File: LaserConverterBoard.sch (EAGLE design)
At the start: 49 parts, among them J10 24V, J11 FAN, J12 E-STOP, J3 04-JST-B4B-XH-A, J4 04-JST-B4B-XH-A, J5 04-JST-B4B-XH-A, J6 X, J7 Y, J8 Z-STOP, Q1 FDN5630, Q2 FDN5630, U10 REE-0505S, Y1 POLOLU_A4988, Y2 POLOLU_A4988, Y3 POLOLU_A4988

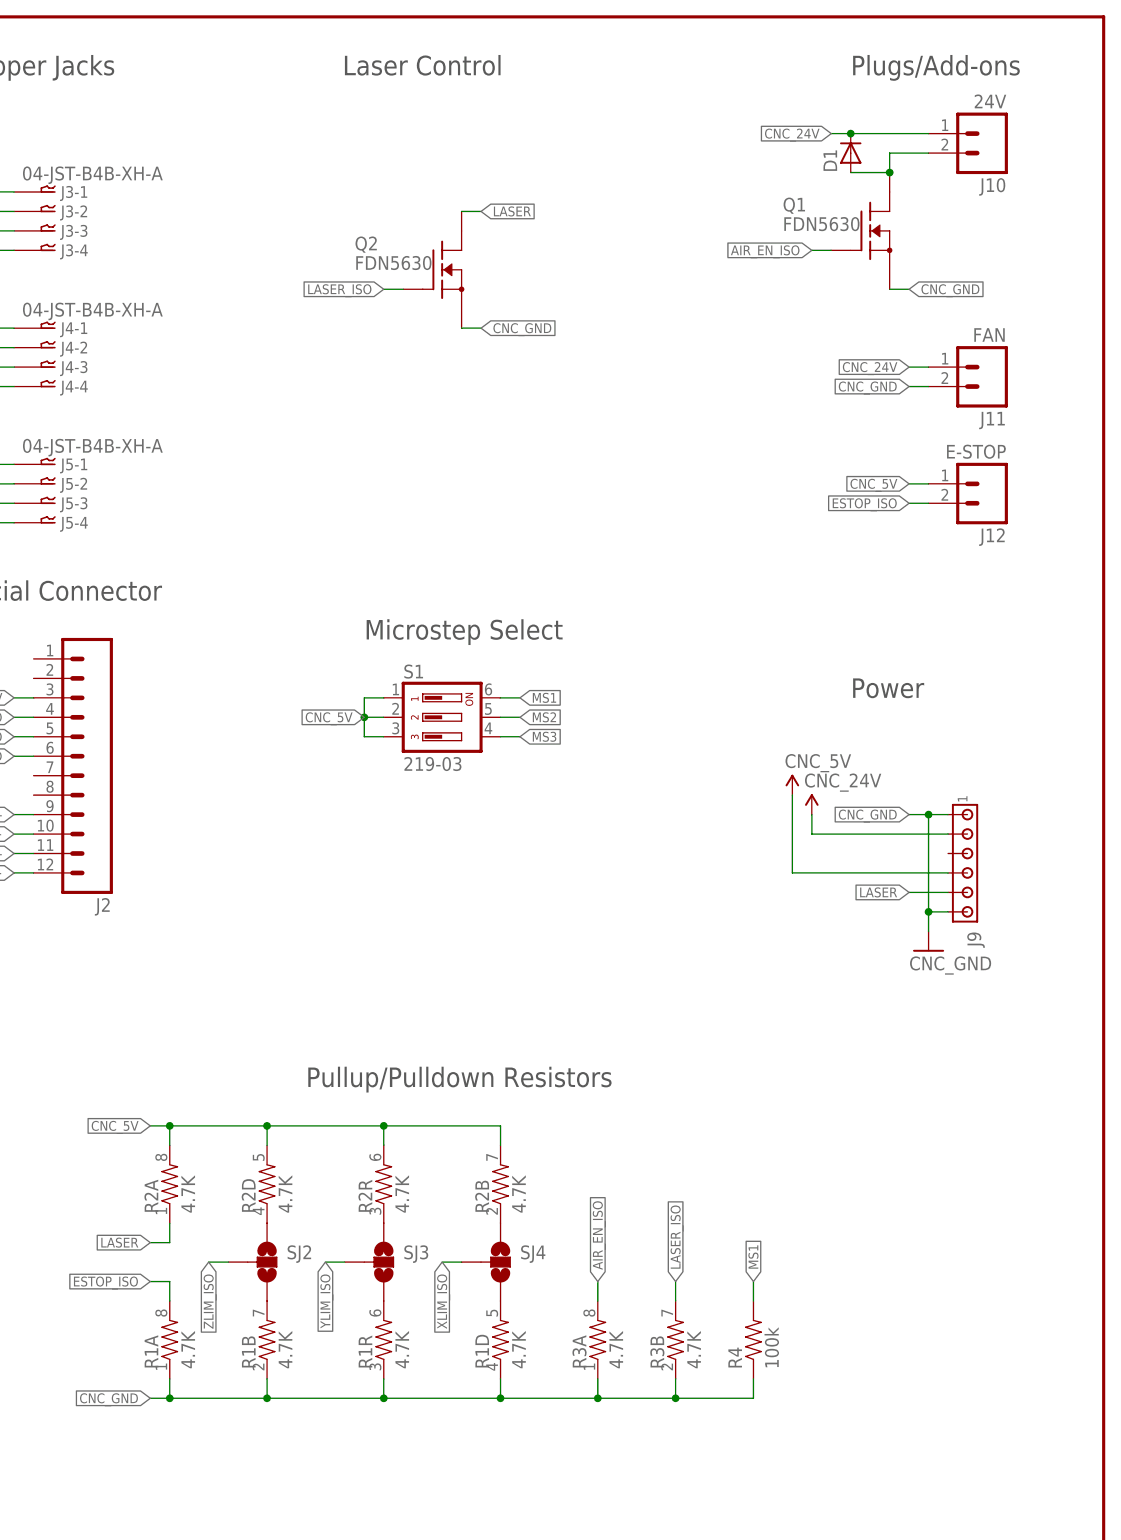
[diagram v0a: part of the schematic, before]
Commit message: Hand routing of board 1.3 complete. Still needs silk screening done.
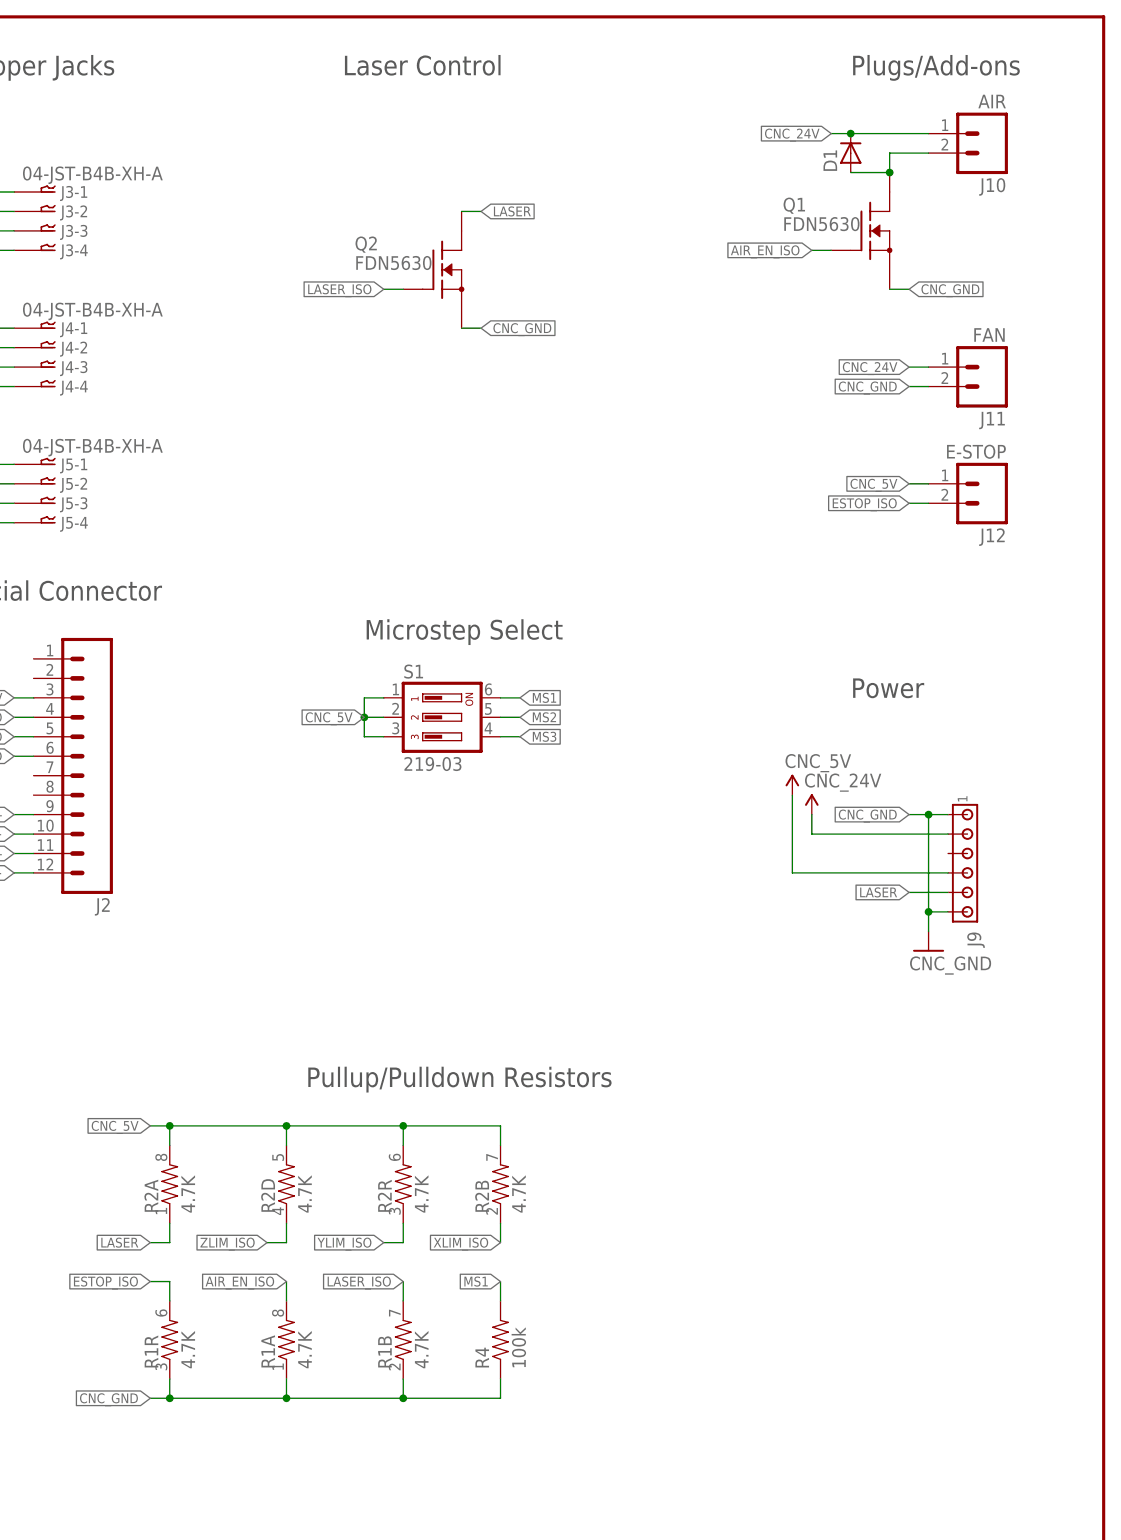
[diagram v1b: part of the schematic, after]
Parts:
- removed R3: 4.7K, SparkFun-Resistors:RESISTOR-ARRAY0603-ARV
- removed SJ2, SJ3, SJ4: (no value), SparkFun-Passives:SOLDERJUMPER_2WAYS
- J10: value 24V -> AIR; device SparkFun-Connectors:M02PTH -> SparkFun-Connectors:M02POLAR
- J11, J12: device SparkFun-Connectors:M02PTH -> SparkFun-Connectors:M02POLAR
- J6, J7: device SparkFun-Connectors:M03PTH -> SparkFun-Connectors:M03POLAR
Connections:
- removed net N$1: R1B.2, SJ2.3
- removed net N$2: R1R.2, SJ3.3
- removed net N$3: R2D.1, SJ2.1
- removed net N$4: R2R.1, SJ3.1
- removed net N$5: R2B.1, SJ4.1
- removed net N$6: R1D.2, SJ4.3
- net AIR_EN_ISO: now also R1A.2; no longer R3A.2
- net CNC_GND: no longer R1D.1, R3A.1, R3B.1
- net ESTOP_ISO: now also R1R.2; no longer R1A.2
- net LASER_ISO: now also R1B.2; no longer R3B.2
- net XLIM_ISO: now also R2B.1; no longer SJ4.2
- net YLIM_ISO: now also R2R.1; no longer SJ3.2
- net ZLIM_ISO: now also R2D.1; no longer SJ2.2
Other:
- moved on the sheet: R1A, R1B, R1R, R2D, R2R, R4

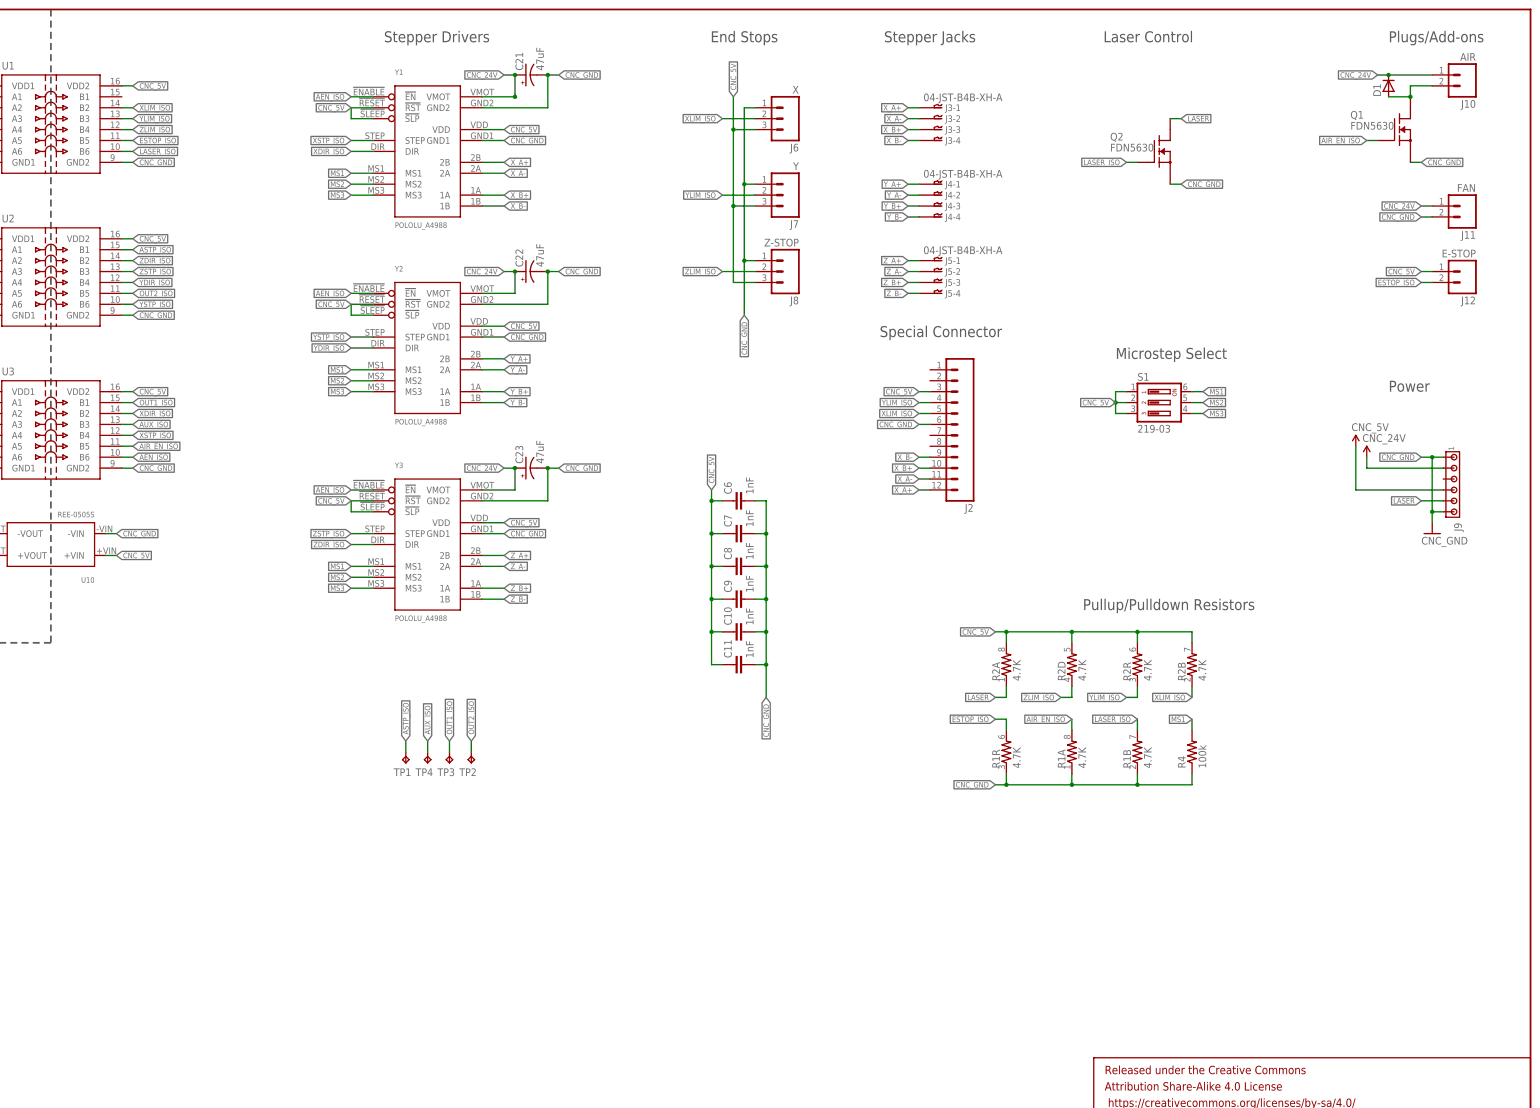
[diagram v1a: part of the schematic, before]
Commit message: Silk screen done, could use a Chimera Logo on it, IMO
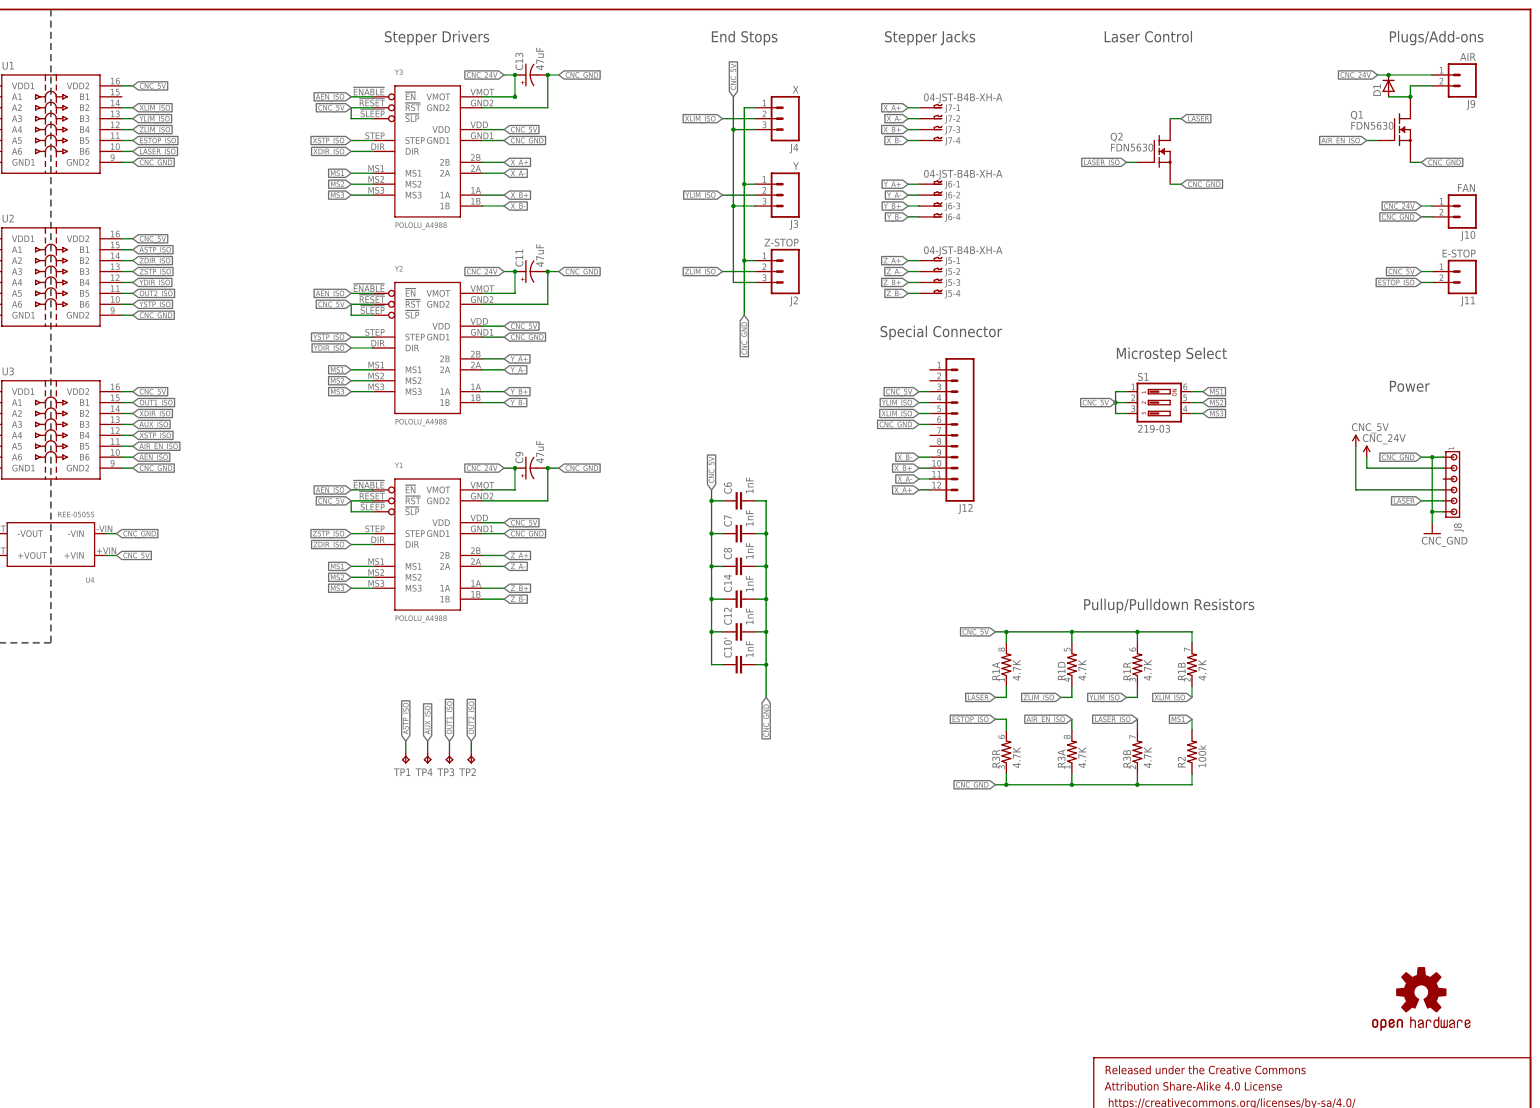
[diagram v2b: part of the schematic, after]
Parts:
- removed C22, C23: 47uF, rcl:CPOL-USE
- removed R4: 100k, SparkFun-Resistors:100KOHM1/10W1%(0603)
- added C10', C14: 1nF, SparkFun-Capacitors:1NF/1000PF-50V-10%(0603)
- added LOGO1: OSHW-LOGOS, SparkFun-Aesthetics:OSHW-LOGOS
- added R3: 4.7K, SparkFun-Resistors:RESISTOR-ARRAY0603-ARV
- C11, C9: value 1nF -> 47uF; device SparkFun-Capacitors:1NF/1000PF-50V-10%(0603) -> rcl:CPOL-USE
- J10: value AIR -> FAN
- J11: value FAN -> E-STOP
- J12: value E-STOP -> (none); device SparkFun-Connectors:M02POLAR -> con-amp-te:M12
- J2: value (none) -> Z-STOP; device con-amp-te:M12 -> SparkFun-Connectors:M03POLAR
- J3: value 04-JST-B4B-XH-A -> Y; device con-jst-xh:04-JST-B4B-XH-A -> SparkFun-Connectors:M03POLAR
- J4: value 04-JST-B4B-XH-A -> X; device con-jst-xh:04-JST-B4B-XH-A -> SparkFun-Connectors:M03POLAR
- J6: value X -> 04-JST-B4B-XH-A; device SparkFun-Connectors:M03POLAR -> con-jst-xh:04-JST-B4B-XH-A
- J7: value Y -> 04-JST-B4B-XH-A; device SparkFun-Connectors:M03POLAR -> con-jst-xh:04-JST-B4B-XH-A
- J8: value Z-STOP -> (none); device SparkFun-Connectors:M03POLAR -> con-amp:MTA06-156
- J9: value (none) -> AIR; device con-amp:MTA06-156 -> SparkFun-Connectors:M02POLAR
- R2: value 4.7K -> 100k; device SparkFun-Resistors:RESISTOR-ARRAY0603-ARV -> SparkFun-Resistors:100KOHM1/10W1%(0603)
- renumbered C10 to C12, C21 to C13, U10 to U4
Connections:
- net AIR_EN_ISO: now also R3A.2; no longer R1A.2
- net CNC_24V: now also C11.+, C9.+, J8.2, J9.1; no longer C22.+, C23.+, J11.1, J9.2
- net CNC_5V: now also C10'.1, C14.1, J11.1, J12.3, J3.3, J4.3, J8.4, R1A.2, R1B.2, R1D.2, R1R.2; no longer C11.1, C9.1, J12.1, J6.3, J7.3, J8.3, J9.4, R2A.2, R2B.2, R2D.2, R2R.2
- net CNC_GND: now also C10'.2, C11.-, C14.2, C9.-, J10.2, J12.6, J2.1, J3.1, J4.1, J8.6, R2.1, R3A.1, R3B.1, R3R.1; no longer C11.2, C22.-, C23.-, C9.2, J11.2, J2.6, J6.1, J7.1, J9.1, J9.6, R1A.1, R1B.1, R1R.1, R4.1
- net ESTOP_ISO: now also J11.2, R3R.2; no longer J12.2, R1R.2
- net LASER: now also J8.5, R1A.1; no longer J9.5, R2A.1
- net LASER_ISO: now also R3B.2; no longer R1B.2
- net MS1: now also R2.2; no longer R4.2
- net N$8: now also J9.2; no longer J10.2
- net XDIR_ISO: now also Y3.DIR; no longer Y1.DIR
- net XLIM_ISO: now also J12.5, J4.2, R1B.1; no longer J2.5, J6.2, R2B.1
- net XSTP_ISO: now also Y3.STEP; no longer Y1.STEP
- net X_A+: now also J12.12, J7-1.1, Y3.2B; no longer J2.12, J3-1.1, Y1.2B
- net X_A-: now also J12.11, J7-2.1, Y3.2A; no longer J2.11, J3-2.1, Y1.2A
- net X_B+: now also J12.10, J7-3.1, Y3.1A; no longer J2.10, J3-3.1, Y1.1A
- net X_B-: now also J12.9, J7-4.1, Y3.1B; no longer J2.9, J3-4.1, Y1.1B
- net YLIM_ISO: now also J12.4, J3.2, R1R.1; no longer J2.4, J7.2, R2R.1
- net Y_A+: now also J6-1.1; no longer J4-1.1
- net Y_A-: now also J6-2.1; no longer J4-2.1
- net Y_B+: now also J6-3.1; no longer J4-3.1
- net Y_B-: now also J6-4.1; no longer J4-4.1
- net ZDIR_ISO: now also Y1.DIR; no longer Y3.DIR
- net ZLIM_ISO: now also J2.2, R1D.1; no longer J8.2, R2D.1
- net ZSTP_ISO: now also Y1.STEP; no longer Y3.STEP
- net Z_A+: now also Y1.2B; no longer Y3.2B
- net Z_A-: now also Y1.2A; no longer Y3.2A
- net Z_B+: now also Y1.1A; no longer Y3.1A
- net Z_B-: now also Y1.1B; no longer Y3.1B
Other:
- moved on the sheet: J10, J11, R1A, R1B, R1R, Y1, Y3

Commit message: More silkscreen and plug fixes to full-size board
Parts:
- J10, J11, J9: device SparkFun-Connectors:M02POLAR -> SparkFun-Connectors:M02PTH
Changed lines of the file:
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@@
 <part name="R3" library="SparkFun-Resistors" deviceset="RESISTOR-ARRAY" device="0603-ARV" value="4.7K"/>
 <part name="R1" library="SparkFun-Resistors" deviceset="RESISTOR-ARRAY" device="0603-ARV" value="4.7K"/>
-<part name="J11" library="SparkFun-Connectors" deviceset="M02" device="POLAR" value="E-STOP"/>
-<part name="J10" library="SparkFun-Connectors" deviceset="M02" device="POLAR" value="FAN"/>
+<part name="J11" library="SparkFun-Connectors" deviceset="M02" device="PTH" value="E-STOP"/>
+<part name="J10" library="SparkFun-Connectors" deviceset="M02" device="PTH" value="FAN"/>
 <part name="Y3" library="pololu" deviceset="POLOLU_A4988" device=""/>
 <part name="Y2" library="pololu" deviceset="POLOLU_A4988" device=""/>
@@
 <part name="J6" library="con-jst-xh" deviceset="04-JST" device="-B4B-XH-A"/>
 <part name="J5" library="con-jst-xh" deviceset="04-JST" device="-B4B-XH-A"/>
-<part name="J9" library="SparkFun-Connectors" deviceset="M02" device="POLAR" value="AIR"/>
+<part name="J9" library="SparkFun-Connectors" deviceset="M02" device="PTH" value="AIR"/>
 <part name="D1" library="semicon-smd-ipc" deviceset="D-" device="SOD123"/>
 <part name="Q1" library="Fairchild_By_element14_Batch_1" deviceset="FDN5630" device="" value="FDN5630"/>
